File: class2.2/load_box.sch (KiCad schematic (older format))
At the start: 4 parts

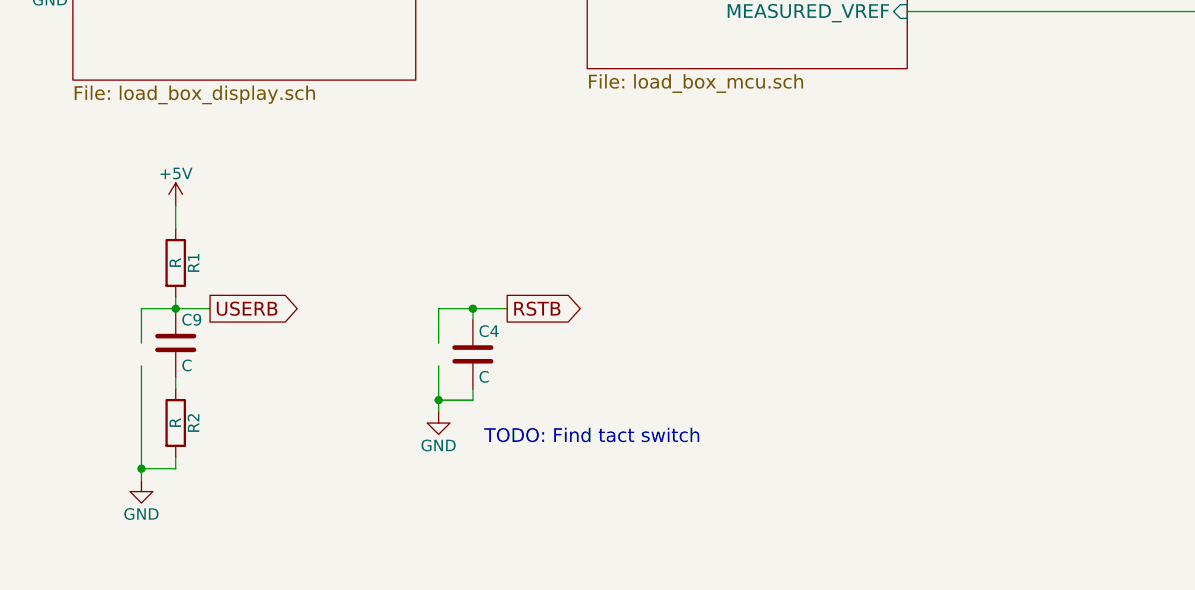
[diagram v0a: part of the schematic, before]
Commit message: Moving class2.2 forward, includes 13V switching converter.
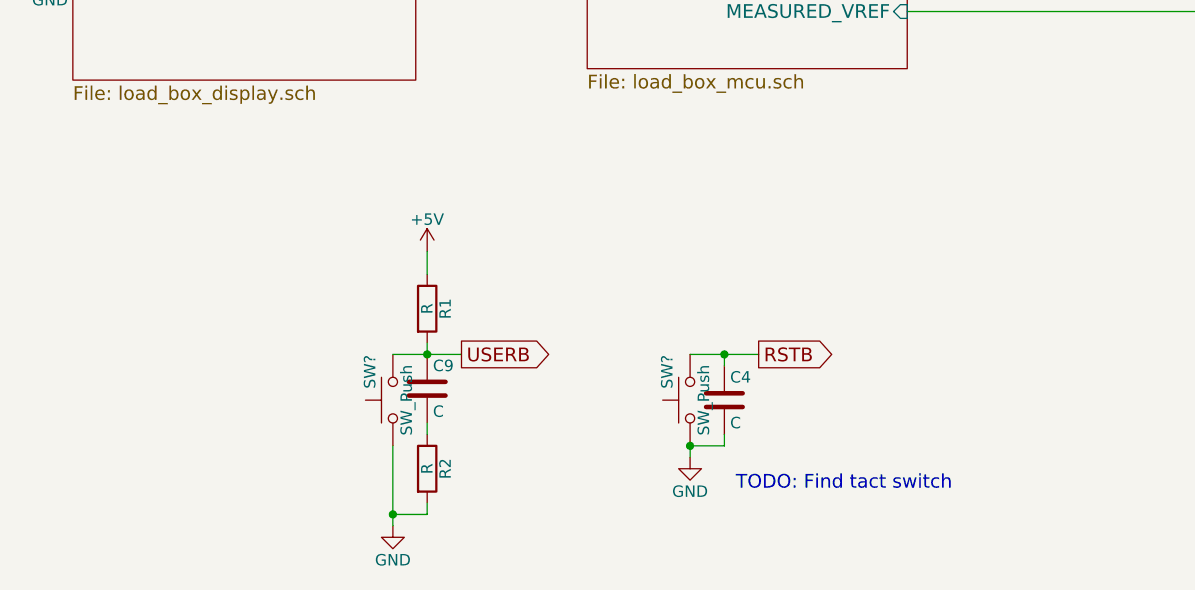
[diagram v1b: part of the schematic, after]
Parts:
- added SW? (x2): SW_Push, Buttons_Switches_SMD:SW_SPST_EVQP2, symbol SW_Push
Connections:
- wire segments 35 -> 33
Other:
- moved on the sheet: C4, C9, R1, R2
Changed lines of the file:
@@
 LIBS:stm32
 LIBS:switches
+LIBS:ap3012
 LIBS:fpc
 LIBS:load_box-cache
@@
 $EndDescr
 $Comp
-L GND #PWR04
+L GND #PWR6
 U 1 1 58EEAE1F
-P 2750 6650
-F 0 "#PWR04" H 2750 6400 50  0001 C CNN
-F 1 "GND" H 2750 6500 50  0000 C CNN
-F 2 "" H 2750 6650 50  0001 C CNN
-F 3 "" H 2750 6650 50  0001 C CNN
-	1    2750 6650
+P 3850 6850
+F 0 "#PWR6" H 3850 6600 50  0001 C CNN
+F 1 "GND" H 3850 6700 50  0000 C CNN
+F 2 "" H 3850 6850 50  0001 C CNN
+F 3 "" H 3850 6850 50  0001 C CNN
+	1    3850 6850
 	1    0    0    -1
 $EndComp
@@
 L C C4
 U 1 1 58EEAE38
-P 2900 6400
-F 0 "C4" H 2925 6500 50  0000 L CNN
-F 1 "C" H 2925 6300 50  0000 L CNN
-F 2 "Capacitors_SMD:C_0603" H 2938 6250 50  0001 C CNN
-F 3 "" H 2900 6400 50  0001 C CNN
-	1    2900 6400
-	1    0    0    -1
-$EndComp
-Text Notes 2950 6800 0    60   ~ 0
+P 4000 6600
+F 0 "C4" H 4025 6700 50  0000 L CNN
+F 1 "C" H 4025 6500 50  0000 L CNN
+F 2 "Capacitors_SMD:C_0603" H 4038 6450 50  0001 C CNN
+F 3 "" H 4000 6600 50  0001 C CNN
+	1    4000 6600
+	1    0    0    -1
+$EndComp
+Text Notes 4050 7000 0    60   ~ 0
 TODO: Find tact switch
 Wire Wire Line
-	2750 6200 3050 6200
-Wire Wire Line
-	2750 6200 2750 6350
-Wire Wire Line
-	2750 6450 2750 6650
-Wire Wire Line
-	2900 6200 2900 6250
-Connection ~ 2900 6200
-Wire Wire Line
-	2900 6550 2900 6600
-Wire Wire Line
-	2900 6600 2750 6600
-Connection ~ 2750 6600
-Text GLabel 3050 6200 2    60   Output ~ 0
+	3850 6400 4150 6400
+Wire Wire Line
+	4000 6400 4000 6450
+Connection ~ 4000 6400
+Wire Wire Line
+	4000 6750 4000 6800
+Wire Wire Line
+	4000 6800 3850 6800
+Connection ~ 3850 6800
+Text GLabel 4150 6400 2    60   Output ~ 0
 RSTB
-Text GLabel 1750 6200 2    60   Output ~ 0
+Text GLabel 2850 6400 2    60   Output ~ 0
 USERB
 Wire Wire Line
-	1450 6200 1750 6200
-Wire Wire Line
-	1450 6200 1450 6350
-Wire Wire Line
-	1450 6450 1450 6950
-$Comp
-L GND #PWR06
+	2550 6400 2850 6400
+$Comp
+L GND #PWR3
 U 1 1 58EEBA66
-P 1450 6950
-F 0 "#PWR06" H 1450 6700 50  0001 C CNN
-F 1 "GND" H 1450 6800 50  0000 C CNN
-F 2 "" H 1450 6950 50  0001 C CNN
-F 3 "" H 1450 6950 50  0001 C CNN
-	1    1450 6950
+P 2550 7150
+F 0 "#PWR3" H 2550 6900 50  0001 C CNN
+F 1 "GND" H 2550 7000 50  0000 C CNN
+F 2 "" H 2550 7150 50  0001 C CNN
+F 3 "" H 2550 7150 50  0001 C CNN
+	1    2550 7150
 	1    0    0    -1
 $EndComp
@@
 L C C9
 U 1 1 58EEBA98
-P 1600 6350
-F 0 "C9" H 1625 6450 50  0000 L CNN
-F 1 "C" H 1625 6250 50  0000 L CNN
-F 2 "Capacitors_SMD:C_0603" H 1638 6200 50  0001 C CNN
-F 3 "" H 1600 6350 50  0001 C CNN
-	1    1600 6350
-	1    0    0    -1
-$EndComp
-$Comp
-L +5V #PWR07
+P 2700 6550
+F 0 "C9" H 2725 6650 50  0000 L CNN
+F 1 "C" H 2725 6450 50  0000 L CNN
+F 2 "Capacitors_SMD:C_0603" H 2738 6400 50  0001 C CNN
+F 3 "" H 2700 6550 50  0001 C CNN
+	1    2700 6550
+	1    0    0    -1
+$EndComp
+$Comp
+L +5V #PWR4
 U 1 1 58EEBB6E
-P 1600 5750
-F 0 "#PWR07" H 1600 5600 50  0001 C CNN
-F 1 "+5V" H 1600 5890 50  0000 C CNN
-F 2 "" H 1600 5750 50  0001 C CNN
-F 3 "" H 1600 5750 50  0001 C CNN
-	1    1600 5750
+P 2700 5950
+F 0 "#PWR4" H 2700 5800 50  0001 C CNN
+F 1 "+5V" H 2700 6090 50  0000 C CNN
+F 2 "" H 2700 5950 50  0001 C CNN
+F 3 "" H 2700 5950 50  0001 C CNN
+	1    2700 5950
 	1    0    0    -1
 $EndComp
@@
 L R R1
 U 1 1 58EEBB9E
-P 1600 6000
-F 0 "R1" V 1680 6000 50  0000 C CNN
-F 1 "R" V 1600 6000 50  0000 C CNN
-F 2 "Resistors_SMD:R_0603" V 1530 6000 50  0001 C CNN
-F 3 "" H 1600 6000 50  0001 C CNN
-	1    1600 6000
-	1    0    0    -1
-$EndComp
-Wire Wire Line
-	1600 5750 1600 5850
-Wire Wire Line
-	1600 6150 1600 6200
-Connection ~ 1600 6200
+P 2700 6200
+F 0 "R1" V 2780 6200 50  0000 C CNN
+F 1 "R" V 2700 6200 50  0000 C CNN
+F 2 "Resistors_SMD:R_0603" V 2630 6200 50  0001 C CNN
+F 3 "" H 2700 6200 50  0001 C CNN
+	1    2700 6200
+	1    0    0    -1
+$EndComp
+Wire Wire Line
+	2700 5950 2700 6050
+Wire Wire Line
+	2700 6350 2700 6400
+Connection ~ 2700 6400
 $Comp
 L R R2
 U 1 1 58EEBD44
-P 1600 6700
-F 0 "R2" V 1680 6700 50  0000 C CNN
-F 1 "R" V 1600 6700 50  0000 C CNN
-F 2 "Resistors_SMD:R_0603" V 1530 6700 50  0001 C CNN
-F 3 "" H 1600 6700 50  0001 C CNN
-	1    1600 6700
-	1    0    0    -1
-$EndComp
-Wire Wire Line
-	1600 6500 1600 6550
-Wire Wire Line
-	1600 6850 1600 6900
-Wire Wire Line
-	1600 6900 1450 6900
-Connection ~ 1450 6900
+P 2700 6900
+F 0 "R2" V 2780 6900 50  0000 C CNN
+F 1 "R" V 2700 6900 50  0000 C CNN
+F 2 "Resistors_SMD:R_0603" V 2630 6900 50  0001 C CNN
+F 3 "" H 2700 6900 50  0001 C CNN
+	1    2700 6900
+	1    0    0    -1
+$EndComp
+Wire Wire Line
+	2700 6700 2700 6750
+Wire Wire Line
+	2700 7050 2700 7100
+Wire Wire Line
+	2700 7100 2550 7100
+Connection ~ 2550 7100
 $Sheet
 S 1150 2850 1500 2350
@@
 	5300 3000 4800 3000
 $Comp
-L +3.3V #PWR?
+L +3.3V #PWR1
 U 1 1 58F00E63
 P 1050 4350
-F 0 "#PWR?" H 1050 4200 50  0001 C CNN
+F 0 "#PWR1" H 1050 4200 50  0001 C CNN
 F 1 "+3.3V" H 1050 4490 50  0000 C CNN
 F 2 "" H 1050 4350 50  0001 C CNN
@@
 $EndComp
 $Comp
-L GND #PWR?
+L GND #PWR2
 U 1 1 58F00F1B
 P 1050 4700
-F 0 "#PWR?" H 1050 4450 50  0001 C CNN
+F 0 "#PWR2" H 1050 4450 50  0001 C CNN
 F 1 "GND" H 1050 4550 50  0000 C CNN
 F 2 "" H 1050 4700 50  0001 C CNN
@@
 	1050 4450 1150 4450
 $Comp
-L GND #PWR?
+L GND #PWR5
 U 1 1 58F0193E
 P 2750 3700
-F 0 "#PWR?" H 2750 3450 50  0001 C CNN
+F 0 "#PWR5" H 2750 3450 50  0001 C CNN
 F 1 "GND" H 2750 3550 50  0000 C CNN
 F 2 "" H 2750 3700 50  0001 C CNN
@@
 Wire Wire Line
 	3400 4250 2650 4250
+$Comp
+L SW_Push SW?
+U 1 1 58F088DD
+P 2550 6600
+F 0 "SW?" H 2600 6700 50  0000 L CNN
+F 1 "SW_Push" H 2550 6540 50  0000 C CNN
+F 2 "Buttons_Switches_SMD:SW_SPST_EVQP2" H 2550 6800 50  0001 C CNN
+F 3 "" H 2550 6800 50  0001 C CNN
+	1    2550 6600
+	0    -1   -1   0
+$EndComp
+$Comp
+L SW_Push SW?
+U 1 1 58F08CF8
+P 3850 6600
+F 0 "SW?" H 3900 6700 50  0000 L CNN
+F 1 "SW_Push" H 3850 6540 50  0000 C CNN
+F 2 "Buttons_Switches_SMD:SW_SPST_EVQP2" H 3850 6800 50  0001 C CNN
+F 3 "" H 3850 6800 50  0001 C CNN
+	1    3850 6600
+	0    -1   -1   0
+$EndComp
+Wire Wire Line
+	3850 6800 3850 6850
+Wire Wire Line
+	2550 6800 2550 7150
 $EndSCHEMATC
